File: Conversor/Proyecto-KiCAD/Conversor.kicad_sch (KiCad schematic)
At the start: 35 parts, among them J1 ConnPila, J2 ConnTrafoP, J3 ConnTrafoS, J4 ConnLf, J5 ConnCarga, Q1 IRFP150, Q2 IRFP150, Q3 IRFP150, Q4 IRFP150

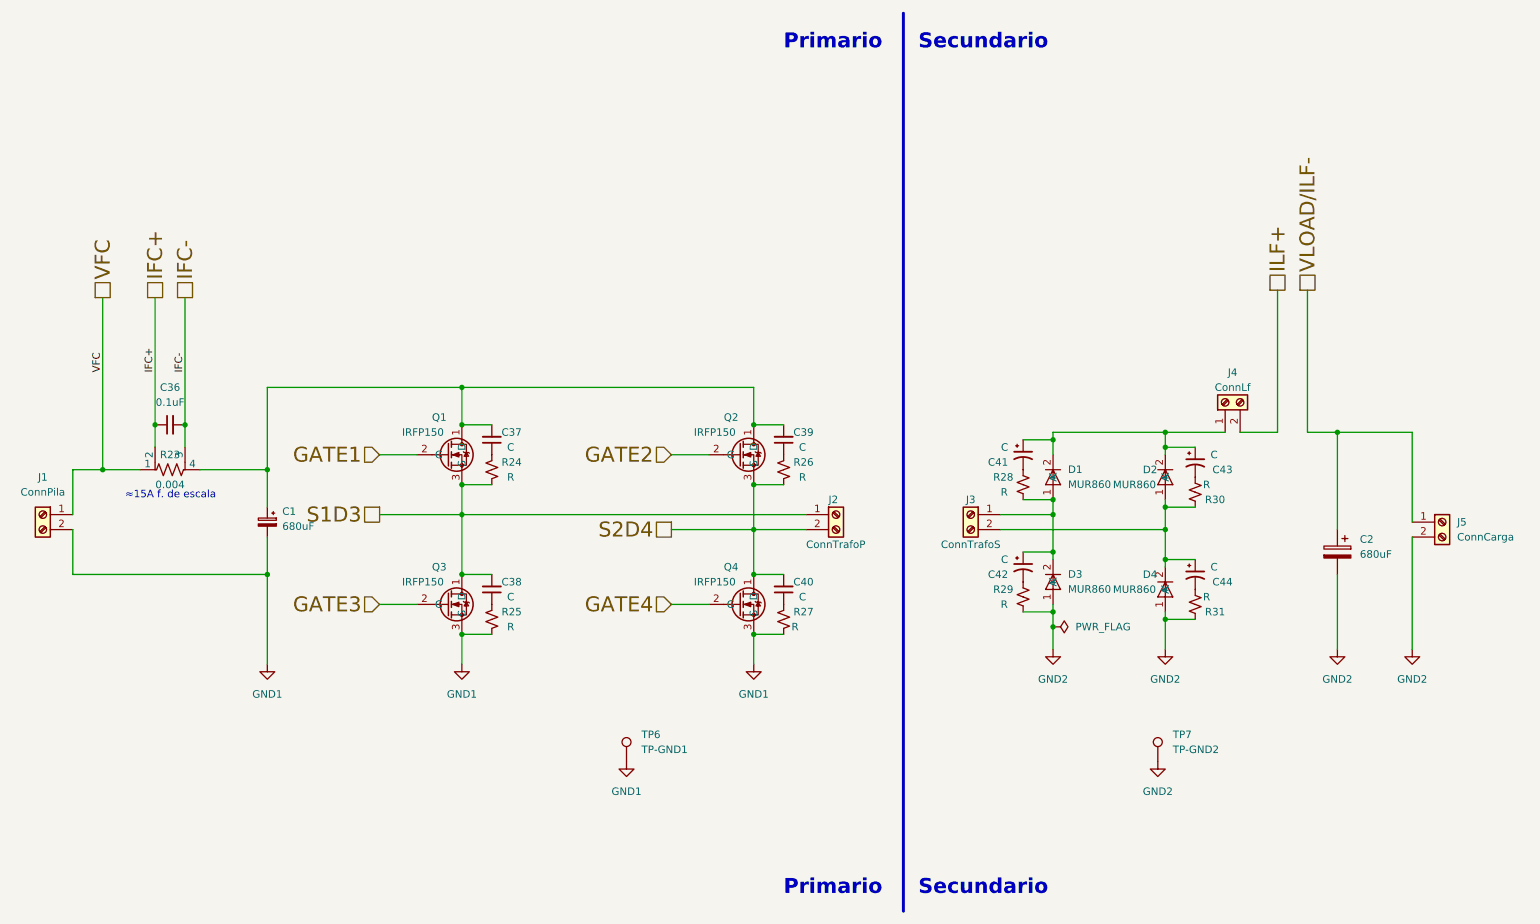
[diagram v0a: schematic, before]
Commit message: Terminar el resto de los cambios de Jorge
- Capacitores electroliticos para el circuito de bootstrap, en paralelo
a los cerámicos
- Cambiar el I2C a 3V3 del lado digital
- Hacer la separacion de linea de datos de I2C del lado digital como en
la nota de aplicación SLYT403A
- Dejar el Vaux del LM5056A con un jumper por si acaso
- Lo mismo con la resistencia de dead-time RDT de los drivers, dejar una
footprint de resistencia SMD para poder cambiarlas de ser necesario
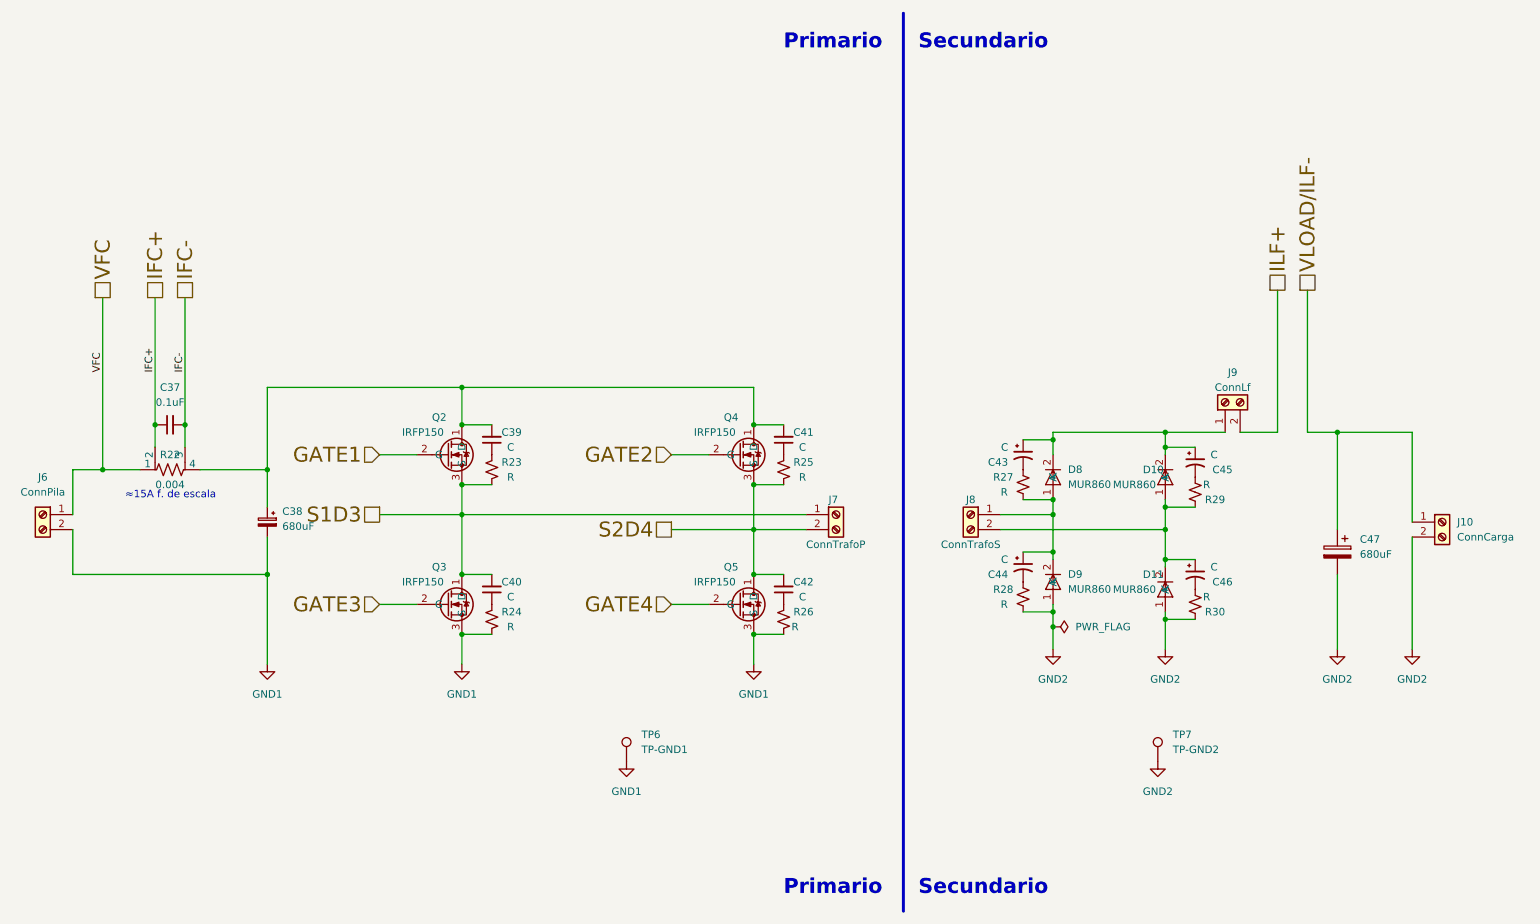
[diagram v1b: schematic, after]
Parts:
- renumbered C36 to C37, C1 to C38, C37 to C39, C38 to C40, C39 to C41, C40 to C42, C41 to C43, C42 to C44, C43 to C45, C44 to C46, C2 to C47, D2 to D10, D4 to D11, D1 to D8, D3 to D9, J5 to J10, J1 to J6, J2 to J7, J3 to J8, J4 to J9, Q1 to Q2, Q2 to Q4, Q4 to Q5, R23 to R22, R24 to R23, R25 to R24, R26 to R25, R27 to R26, R28 to R27, R29 to R28, R30 to R29, R31 to R30

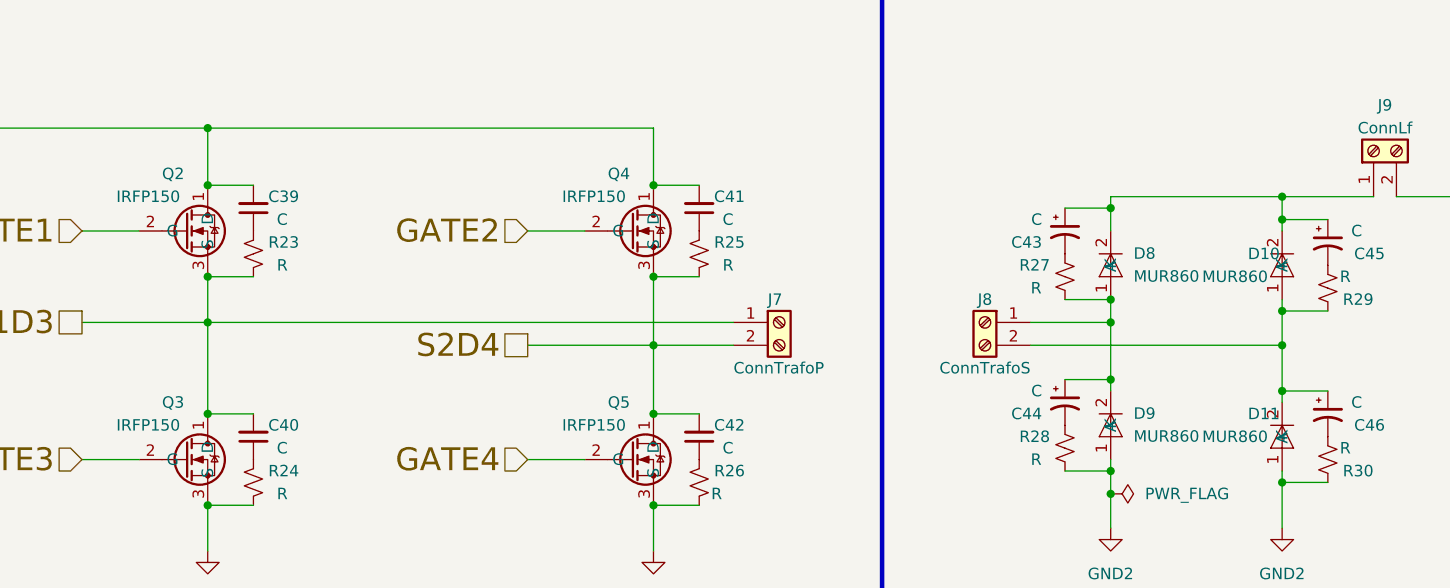
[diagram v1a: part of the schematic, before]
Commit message: Finalizar la PCB y mandarla a fabricar
- Agregar cambios sugeridos por Jorge el 2022/07/22
- Bloqueados todos los componentes de la PCB (no modificar más)
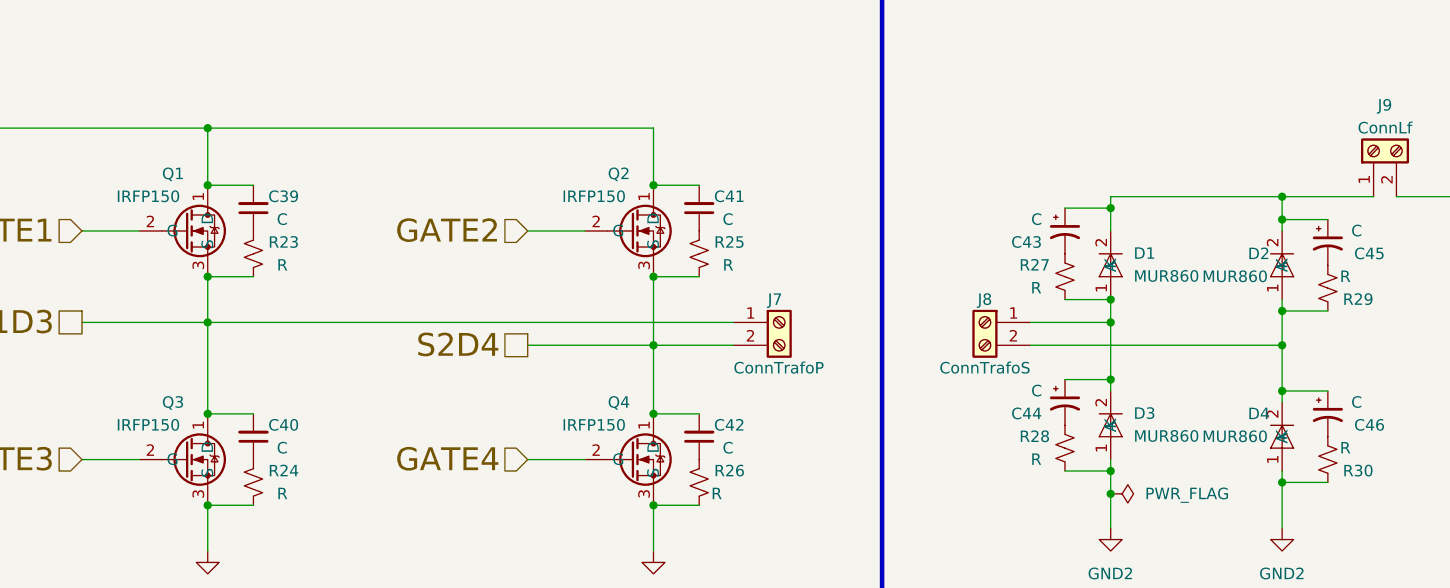
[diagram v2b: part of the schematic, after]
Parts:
- renumbered D8 to D1, D10 to D2, D9 to D3, D11 to D4, Q2 to Q1, Q4 to Q2, Q5 to Q4
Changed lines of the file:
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@@
   (symbol (lib_id "Componentes proyecto:IRFP150") (at 104.14 86.36 0) (unit 1)
     (in_bom yes) (on_board yes)
-    (property "Reference" "Q2" (id 0) (at 99.06 81.28 0)
+    (property "Reference" "Q1" (id 0) (at 99.06 81.28 0)
       (effects (font (size 1.27 1.27)) (justify left))
     )
@@
   (symbol (lib_id "Componentes proyecto:IRFP150") (at 153.67 111.76 0) (unit 1)
     (in_bom yes) (on_board yes)
-    (property "Reference" "Q5" (id 0) (at 148.59 106.68 0)
+    (property "Reference" "Q4" (id 0) (at 148.59 106.68 0)
       (effects (font (size 1.27 1.27)) (justify left))
     )
@@
   (symbol (lib_id "Componentes proyecto:MUR860") (at 204.47 109.22 0) (unit 1)
     (in_bom yes) (on_board yes) (fields_autoplaced)
-    (property "Reference" "D9" (id 0) (at 207.01 107.9118 0)
+    (property "Reference" "D3" (id 0) (at 207.01 107.9118 0)
       (effects (font (size 1.27 1.27)) (justify left))
     )
@@
   (symbol (lib_name "MUR860_1") (lib_id "Componentes proyecto:MUR860") (at 204.47 91.44 0) (unit 1)
     (in_bom yes) (on_board yes) (fields_autoplaced)
-    (property "Reference" "D8" (id 0) (at 207.01 90.1318 0)
+    (property "Reference" "D1" (id 0) (at 207.01 90.1318 0)
       (effects (font (size 1.27 1.27)) (justify left))
     )
@@
   (symbol (lib_name "MUR860_2") (lib_id "Componentes proyecto:MUR860") (at 223.52 91.44 0) (unit 1)
     (in_bom yes) (on_board yes)
-    (property "Reference" "D10" (id 0) (at 219.71 90.17 0)
+    (property "Reference" "D2" (id 0) (at 219.71 90.17 0)
       (effects (font (size 1.27 1.27)) (justify left))
     )
@@
   (symbol (lib_id "Componentes proyecto:IRFP150") (at 153.67 86.36 0) (unit 1)
     (in_bom yes) (on_board yes)
-    (property "Reference" "Q4" (id 0) (at 148.59 81.28 0)
+    (property "Reference" "Q2" (id 0) (at 148.59 81.28 0)
       (effects (font (size 1.27 1.27)) (justify left))
     )
@@
   (symbol (lib_name "MUR860_3") (lib_id "Componentes proyecto:MUR860") (at 223.52 110.49 0) (unit 1)
     (in_bom yes) (on_board yes)
-    (property "Reference" "D11" (id 0) (at 219.71 107.95 0)
-      (effects (font (size 1.27 1.27)) (justify left))
-    )
+    (property "Reference" "D4" (id 0) (at 219.71 107.95 0)
+      (effects (font (size 1.27 1.27)) (justify left))
+    )
